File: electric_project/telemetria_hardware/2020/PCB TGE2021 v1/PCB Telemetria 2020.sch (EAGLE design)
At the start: 19 parts, among them IC1 INA240A1DR, IC2 MCP3221A6T-E_OTVAO, IC3 AZ1117IH-3.3TRG1, IC4 ACS758LCB-050B-PFF-T

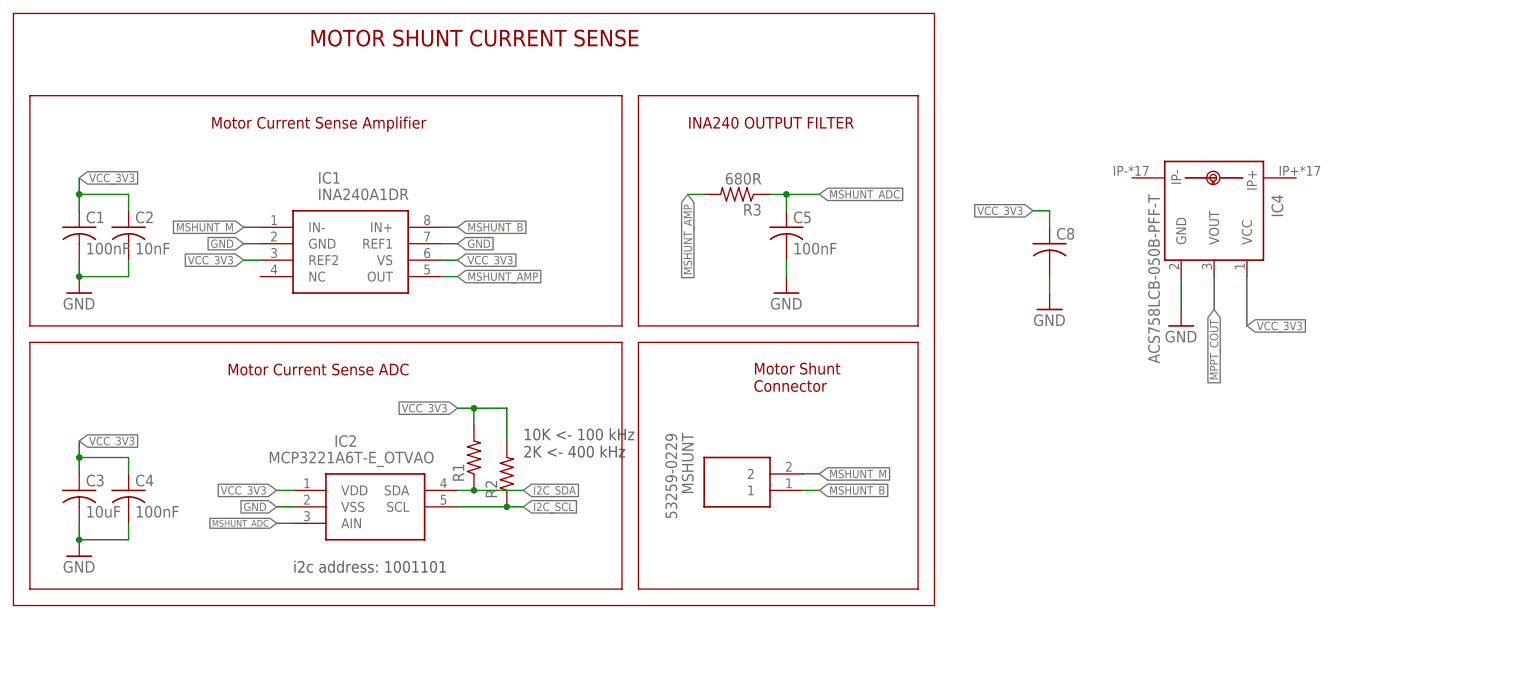
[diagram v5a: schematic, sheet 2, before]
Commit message: Just updating past commit (MPPT current measurement)
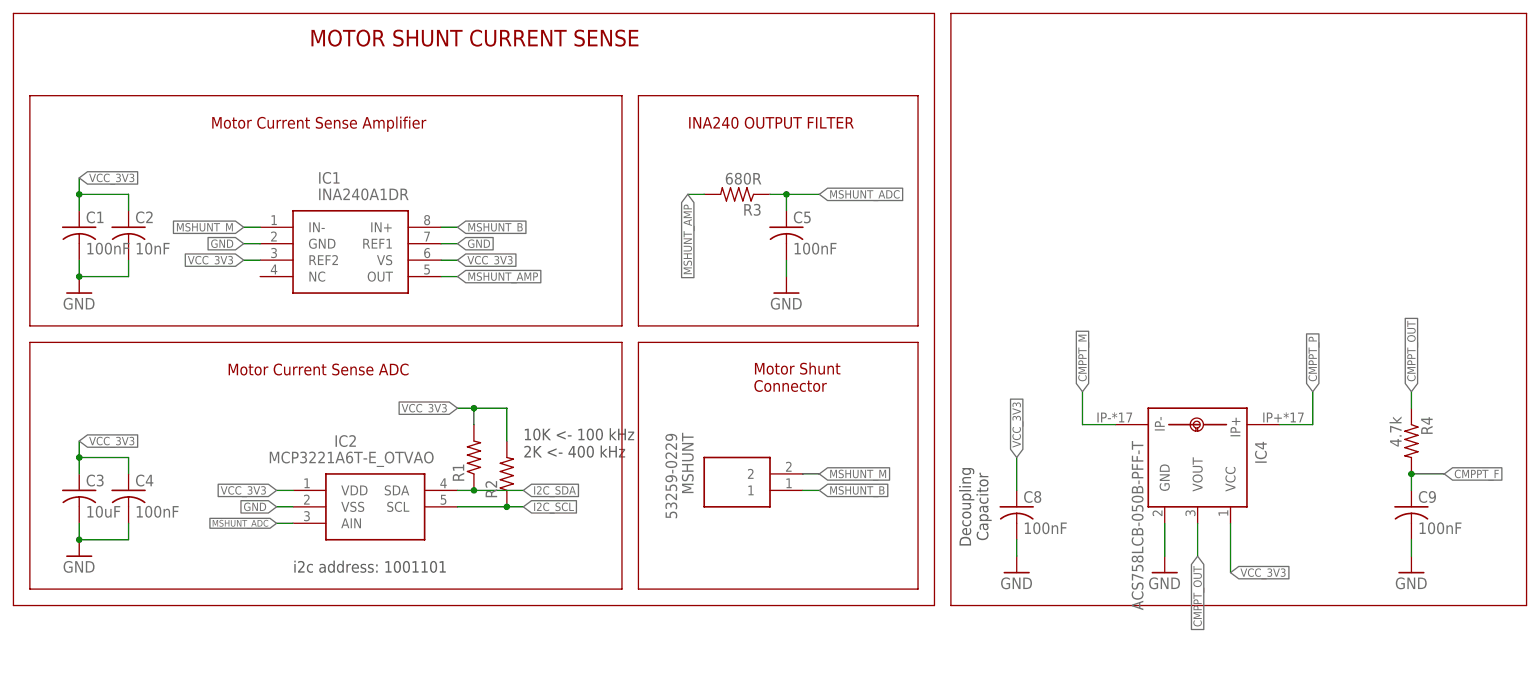
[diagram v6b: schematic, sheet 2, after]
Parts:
- added C9: 100nF, rcl:C-USC0805
- added R4: 4.7k, rcl:R-US_R0805
- C8: value (none) -> 100nF
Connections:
- removed net MPPT_COUT: IC4.VOUT
- new net CMPPT_F: C9.1, R4.2
- new net CMPPT_M: IC4.IP-
- new net CMPPT_OUT: IC4.VOUT, R4.1
- new net CMPPT_P: IC4.IP+
- net GND: now also C9.2
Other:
- note added: "Decoupling Capacitor"
- moved on the sheet: C8, IC4
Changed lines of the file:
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@@
 <part name="IC4" library="allegro" library_urn="urn:adsk.eagle:library:93" deviceset="ACS758*" device="" package3d_urn="urn:adsk.eagle:package:3449/1" technology="LCB-050B-PFF-T"/>
 <part name="GND6" library="supply1" library_urn="urn:adsk.eagle:library:371" deviceset="GND" device=""/>
-<part name="C8" library="rcl" library_urn="urn:adsk.eagle:library:334" deviceset="C-US" device="C0805" package3d_urn="urn:adsk.eagle:package:23617/2"/>
+<part name="C8" library="rcl" library_urn="urn:adsk.eagle:library:334" deviceset="C-US" device="C0805" package3d_urn="urn:adsk.eagle:package:23617/2" value="100nF"/>
 <part name="GND7" library="supply1" library_urn="urn:adsk.eagle:library:371" deviceset="GND" device=""/>
+<part name="C9" library="rcl" library_urn="urn:adsk.eagle:library:334" deviceset="C-US" device="C0805" package3d_urn="urn:adsk.eagle:package:23617/2" value="100nF"/>
+<part name="R4" library="rcl" library_urn="urn:adsk.eagle:library:334" deviceset="R-US_" device="R0805" package3d_urn="urn:adsk.eagle:package:23553/2" value="4.7k"/>
+<part name="GND8" library="supply1" library_urn="urn:adsk.eagle:library:371" deviceset="GND" device=""/>
 </parts>
 <sheets>
@@
 <wire x1="152.4" y1="233.68" x2="109.22" y2="233.68" width="0.1524" layer="94"/>
 <text x="116.84" y="228.6" size="1.778" layer="94">INA240 OUTPUT FILTER</text>
+<wire x1="157.48" y1="246.38" x2="157.48" y2="154.94" width="0.1524" layer="94"/>
+<wire x1="157.48" y1="154.94" x2="246.38" y2="154.94" width="0.1524" layer="94"/>
+<wire x1="246.38" y1="154.94" x2="246.38" y2="246.38" width="0.1524" layer="94"/>
+<wire x1="246.38" y1="246.38" x2="157.48" y2="246.38" width="0.1524" layer="94"/>
+<text x="161.036" y="170.18" size="1.778" layer="97" rot="R90" align="center">Decoupling
+Capacitor</text>
 </plain>
 <instances>
@@
 <attribute name="VALUE" x="129.54" y="200.66" size="1.778" layer="96"/>
 </instance>
-<instance part="IC4" gate="G$1" x="198.12" y="215.9" smashed="yes" rot="R270">
-<attribute name="NAME" x="207.01" y="218.44" size="1.778" layer="95" rot="R270"/>
-<attribute name="VALUE" x="187.96" y="218.44" size="1.778" layer="96" rot="R270"/>
-</instance>
-<instance part="GND6" gate="1" x="193.04" y="198.12" smashed="yes">
-<attribute name="VALUE" x="190.5" y="195.58" size="1.778" layer="96"/>
-</instance>
-<instance part="C8" gate="G$1" x="172.72" y="210.82" smashed="yes">
-<attribute name="NAME" x="173.736" y="211.455" size="1.778" layer="95"/>
-<attribute name="VALUE" x="173.736" y="206.629" size="1.778" layer="96"/>
-</instance>
-<instance part="GND7" gate="1" x="172.72" y="200.66" smashed="yes">
-<attribute name="VALUE" x="170.18" y="198.12" size="1.778" layer="96"/>
+<instance part="IC4" gate="G$1" x="195.58" y="177.8" smashed="yes" rot="R270">
+<attribute name="NAME" x="204.47" y="180.34" size="1.778" layer="95" rot="R270"/>
+<attribute name="VALUE" x="185.42" y="180.34" size="1.778" layer="96" rot="R270"/>
+</instance>
+<instance part="GND6" gate="1" x="190.5" y="160.02" smashed="yes">
+<attribute name="VALUE" x="187.96" y="157.48" size="1.778" layer="96"/>
+</instance>
+<instance part="C8" gate="G$1" x="167.64" y="170.18" smashed="yes">
+<attribute name="NAME" x="168.656" y="170.815" size="1.778" layer="95"/>
+<attribute name="VALUE" x="168.656" y="165.989" size="1.778" layer="96"/>
+</instance>
+<instance part="GND7" gate="1" x="167.64" y="160.02" smashed="yes">
+<attribute name="VALUE" x="165.1" y="157.48" size="1.778" layer="96"/>
+</instance>
+<instance part="C9" gate="G$1" x="228.6" y="170.18" smashed="yes">
+<attribute name="NAME" x="229.616" y="170.815" size="1.778" layer="95"/>
+<attribute name="VALUE" x="229.616" y="165.989" size="1.778" layer="96"/>
+</instance>
+<instance part="R4" gate="G$1" x="228.6" y="180.34" smashed="yes" rot="R270">
+<attribute name="NAME" x="230.0986" y="184.15" size="1.778" layer="95" rot="R270"/>
+<attribute name="VALUE" x="225.298" y="184.15" size="1.778" layer="96" rot="R270"/>
+</instance>
+<instance part="GND8" gate="1" x="228.6" y="160.02" smashed="yes">
+<attribute name="VALUE" x="226.06" y="157.48" size="1.778" layer="96"/>
 </instance>
 </instances>
@@
 <pinref part="IC4" gate="G$1" pin="GND"/>
 <pinref part="GND6" gate="1" pin="GND"/>
-<wire x1="193.04" y1="205.74" x2="193.04" y2="200.66" width="0.1524" layer="91"/>
+<wire x1="190.5" y1="167.64" x2="190.5" y2="162.56" width="0.1524" layer="91"/>
 </segment>
 <segment>
 <pinref part="C8" gate="G$1" pin="2"/>
-<wire x1="172.72" y1="205.74" x2="172.72" y2="203.2" width="0.1524" layer="91"/>
+<wire x1="167.64" y1="165.1" x2="167.64" y2="162.56" width="0.1524" layer="91"/>
 <pinref part="GND7" gate="1" pin="GND"/>
+</segment>
+<segment>
+<pinref part="GND8" gate="1" pin="GND"/>
+<pinref part="C9" gate="G$1" pin="2"/>
+<wire x1="228.6" y1="162.56" x2="228.6" y2="165.1" width="0.1524" layer="91"/>
 </segment>
 </net>
@@
 <segment>
 <pinref part="IC4" gate="G$1" pin="VCC"/>
-<label x="203.2" y="198.12" size="1.27" layer="95" xref="yes"/>
-<wire x1="203.2" y1="198.12" x2="203.2" y2="205.74" width="0.1524" layer="91"/>
+<label x="200.66" y="160.02" size="1.27" layer="95" xref="yes"/>
+<wire x1="200.66" y1="160.02" x2="200.66" y2="167.64" width="0.1524" layer="91"/>
 </segment>
 <segment>
 <pinref part="C8" gate="G$1" pin="1"/>
-<wire x1="172.72" y1="213.36" x2="172.72" y2="215.9" width="0.1524" layer="91"/>
-<wire x1="172.72" y1="215.9" x2="170.18" y2="215.9" width="0.1524" layer="91"/>
-<label x="170.18" y="215.9" size="1.27" layer="95" rot="R180" xref="yes"/>
+<wire x1="167.64" y1="172.72" x2="167.64" y2="177.8" width="0.1524" layer="91"/>
+<label x="167.64" y="177.8" size="1.27" layer="95" rot="R90" xref="yes"/>
 </segment>
 </net>
@@
 </segment>
 </net>
-<net name="MPPT_COUT" class="0">
+<net name="CMPPT_OUT" class="0">
 <segment>
 <pinref part="IC4" gate="G$1" pin="VOUT"/>
-<wire x1="198.12" y1="205.74" x2="198.12" y2="200.66" width="0.1524" layer="91"/>
-<label x="198.12" y="200.66" size="1.27" layer="95" rot="R270" xref="yes"/>
-</segment>
-</net>
+<wire x1="195.58" y1="167.64" x2="195.58" y2="162.56" width="0.1524" layer="91"/>
+<label x="195.58" y="162.56" size="1.27" layer="95" rot="R270" xref="yes"/>
+</segment>
+<segment>
+<pinref part="R4" gate="G$1" pin="1"/>
+<wire x1="228.6" y1="185.42" x2="228.6" y2="187.96" width="0.1524" layer="91"/>
+<label x="228.6" y="187.96" size="1.27" layer="95" rot="R90" xref="yes"/>
+</segment>
+</net>
+<net name="CMPPT_P" class="0">
+<segment>
+<pinref part="IC4" gate="G$1" pin="IP+"/>
+<wire x1="208.28" y1="182.88" x2="213.36" y2="182.88" width="0.1524" layer="91"/>
+<wire x1="213.36" y1="182.88" x2="213.36" y2="187.96" width="0.1524" layer="91"/>
+<label x="213.36" y="187.96" size="1.27" layer="95" rot="R90" xref="yes"/>
+</segment>
+</net>
+<net name="CMPPT_M" class="0">
+<segment>
+<pinref part="IC4" gate="G$1" pin="IP-"/>
+<wire x1="182.88" y1="182.88" x2="177.8" y2="182.88" width="0.1524" layer="91"/>
+<wire x1="177.8" y1="182.88" x2="177.8" y2="187.96" width="0.1524" layer="91"/>
+<label x="177.8" y="187.96" size="1.27" layer="95" rot="R90" xref="yes"/>
+</segment>
+</net>
+<net name="CMPPT_F" class="0">
+<segment>
+<pinref part="C9" gate="G$1" pin="1"/>
+<pinref part="R4" gate="G$1" pin="2"/>
+<wire x1="228.6" y1="172.72" x2="228.6" y2="175.26" width="0.1524" layer="91"/>
+<wire x1="228.6" y1="175.26" x2="233.68" y2="175.26" width="0.1524" layer="91"/>
+<junction x="228.6" y="175.26"/>
+<label x="233.68" y="175.26" size="1.27" layer="95" xref="yes"/>
+</segment>
+</net>
